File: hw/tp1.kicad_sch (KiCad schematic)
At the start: 27 parts

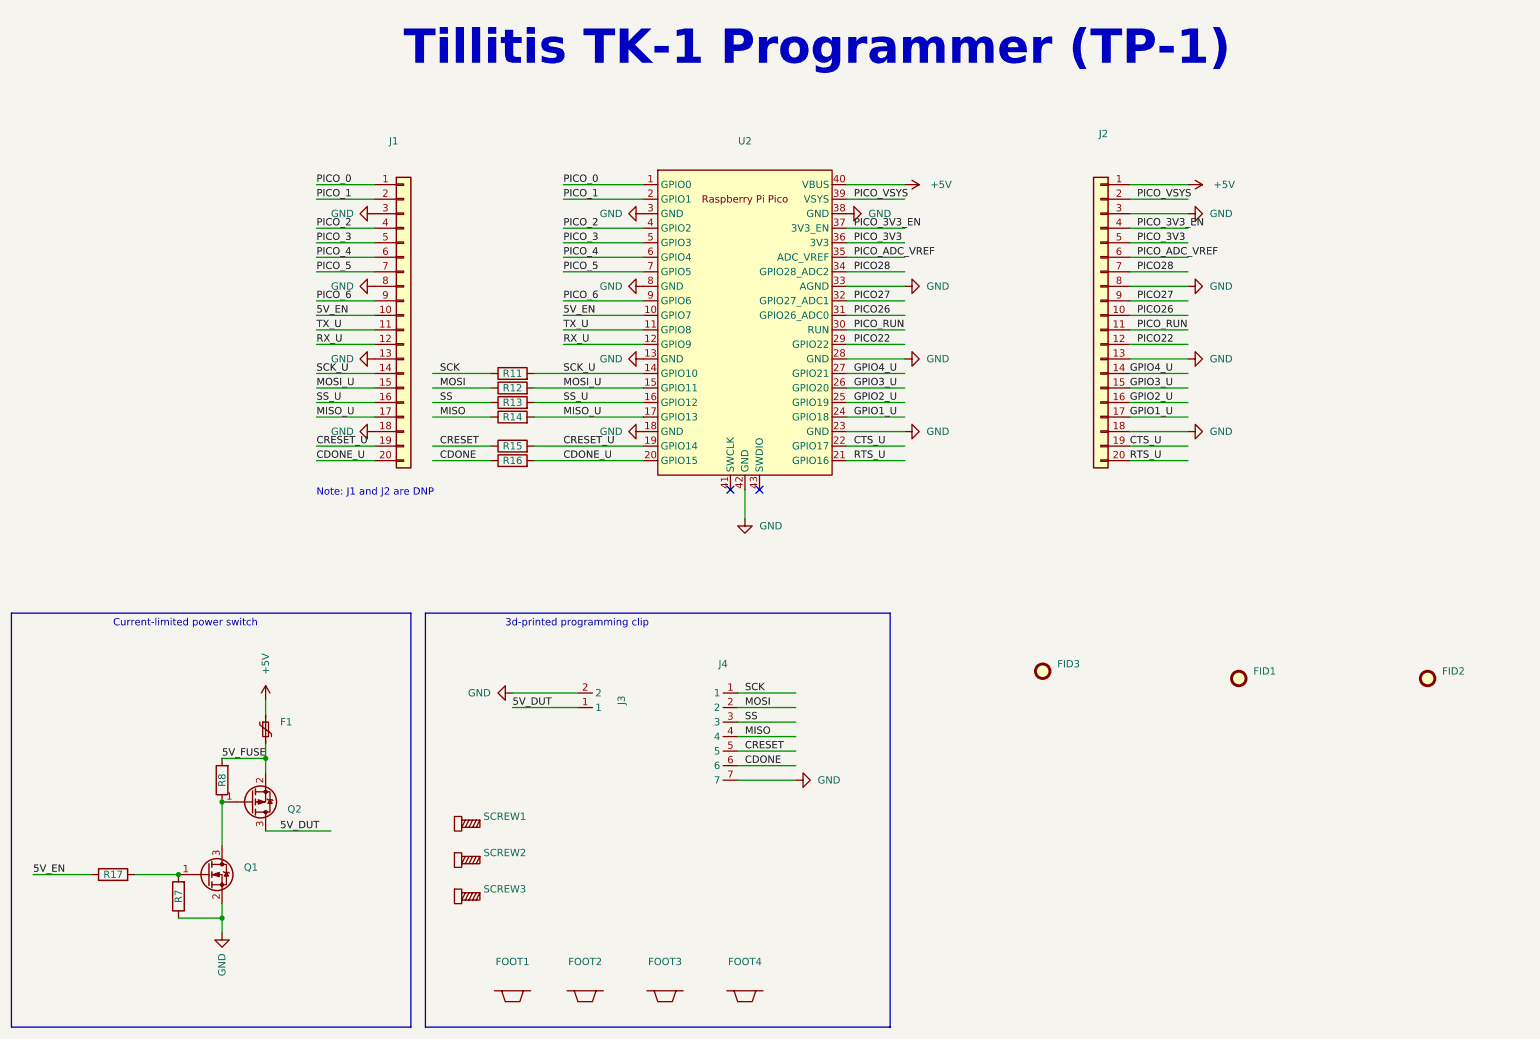
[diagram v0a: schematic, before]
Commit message: Added mta1-library and updated project links
- Updated links to symbols, footprints, drawsheet, 3D models
- Made the links use project defines instead of being absolute
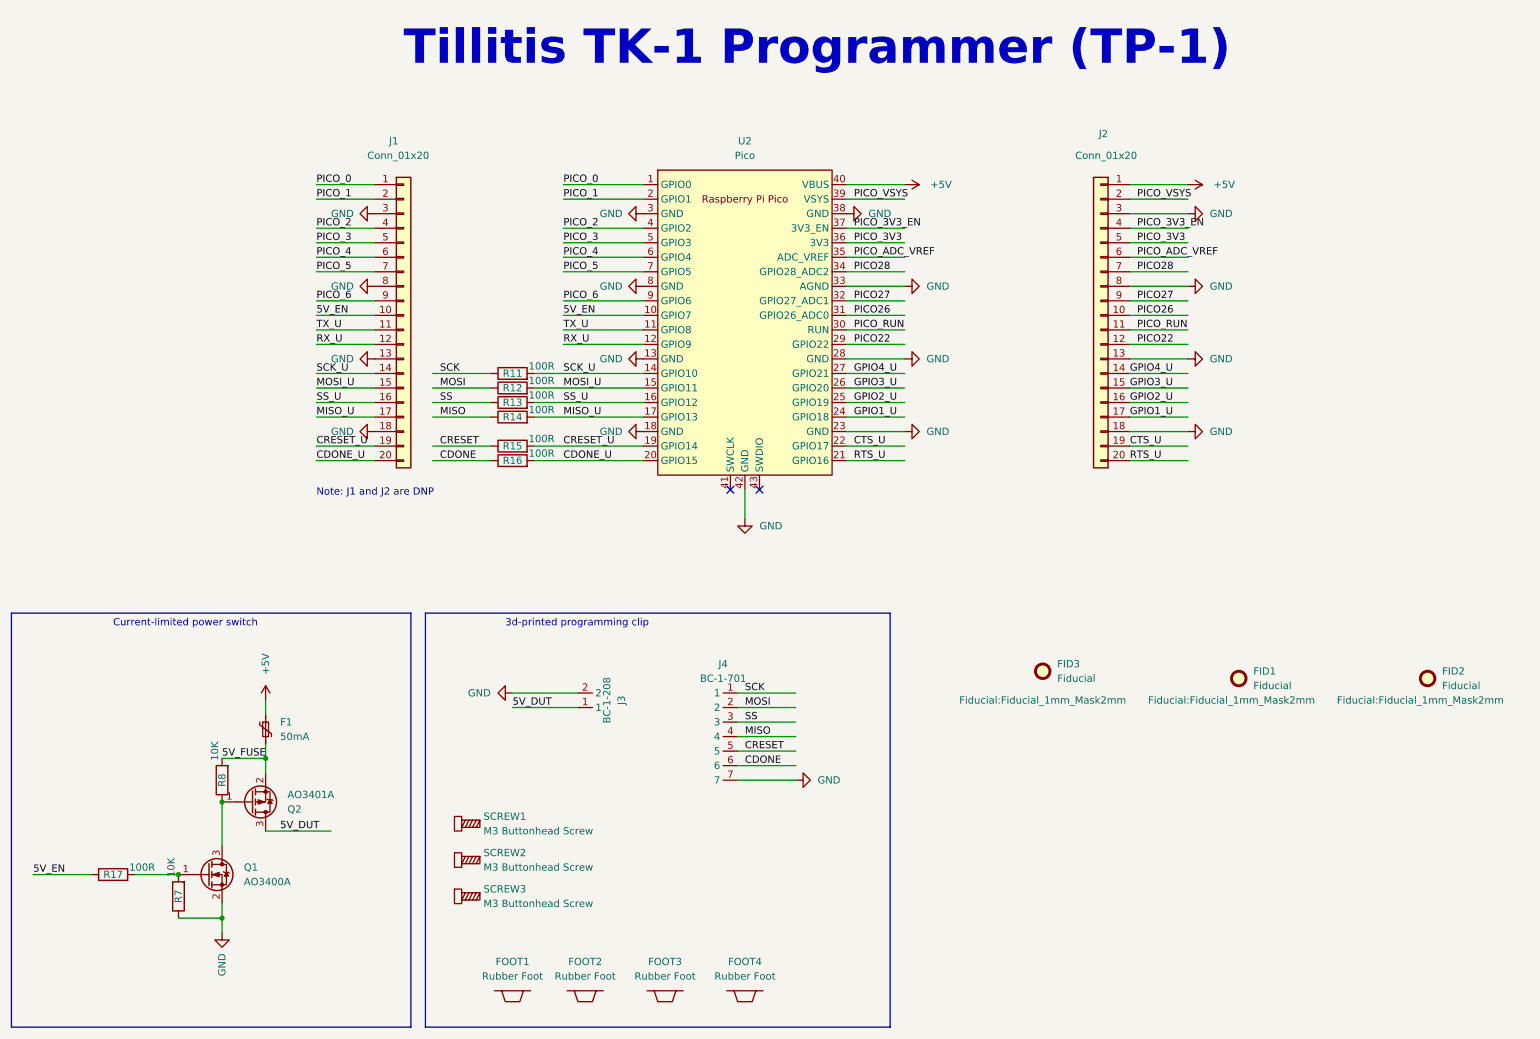
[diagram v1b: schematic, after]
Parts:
- F1: value (none) -> 50mA; footprint (none) -> Fuse:Fuse_1206_3216Metric
- FID1, FID2, FID3: value (none) -> Fiducial; footprint (none) -> Fiducial:Fiducial_1mm_Mask2mm
- FOOT1, FOOT2, FOOT3, FOOT4: value (none) -> Rubber Foot
- J1, J2: value (none) -> Conn_01x20; footprint (none) -> Connector_PinHeader_2.54mm:PinHeader_1x20_P2.54mm_Vertical
- J3: value (none) -> BC-1-208; footprint (none) -> mta1:BC-1-208
- J4: value (none) -> BC-1-701; footprint (none) -> mta1:BC-1-701
- Q1: value (none) -> AO3400A; footprint (none) -> Package_TO_SOT_SMD:SOT-23
- Q2: value (none) -> AO3401A; footprint (none) -> Package_TO_SOT_SMD:SOT-23
- R11, R12, R13, R14, R15, R16, R17: value (none) -> 100R; footprint (none) -> mta1:ERJ2G(0402)_L
- R7, R8: value (none) -> 10K; footprint (none) -> mta1:ERJ2G(0402)_L
- SCREW1, SCREW2, SCREW3: value (none) -> M3 Buttonhead Screw
- U2: value (none) -> Pico; footprint (none) -> MCU_RaspberryPi_and_Boards:RPi_Pico_SMD_reflow

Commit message: Fix all ERC errors.
- Update symbols
- Add PWR_FLAG
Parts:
- U2: footprint MCU_RaspberryPi_and_Boards:RPi_Pico_SMD_reflow -> RPi_Pico:RPi_Pico_SMD_TH
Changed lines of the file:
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@@
     (comment 2 "https://github.com/tillitis/tp1")
   )
+  (junction (at 143.51 104.14) (diameter 0) (color 0 0 0 0)
+  )
   (junction (at 52.07 173.99) (diameter 0) (color 0 0 0 0)
   )
   (junction (at 44.45 166.37) (diameter 0) (color 0 0 0 0)
+  )
+  (junction (at 165.1 45.72) (diameter 0) (color 0 0 0 0)
   )
   (junction (at 52.07 153.67) (diameter 0) (color 0 0 0 0)
@@
     (stroke (width 0) (type default))
   )
-  (wire (pts (xy 161.29 58.42) (xy 171.45 58.42))
+  (wire (pts (xy 161.29 58.42) (xy 176.53 58.42))
     (stroke (width 0) (type default))
   )
@@
     (stroke (width 0) (type default))
   )
+  (wire (pts (xy 161.29 55.88) (xy 176.53 55.88))
+    (stroke (width 0) (type default))
+  )
   (wire (pts (xy 88.9 81.28) (xy 99.06 81.28))
     (stroke (width 0) (type default))
@@
     (stroke (width 0) (type default))
   )
-  (wire (pts (xy 161.29 48.26) (xy 171.45 48.26))
+  (wire (pts (xy 161.29 48.26) (xy 176.53 48.26))
     (stroke (width 0) (type default))
   )
@@
     (stroke (width 0) (type default))
   )
-  (wire (pts (xy 161.29 55.88) (xy 171.45 55.88))
-    (stroke (width 0) (type default))
-  )
   (wire (pts (xy 161.29 83.82) (xy 171.45 83.82))
     (stroke (width 0) (type default))
@@
     (stroke (width 0) (type default))
   )
-  (wire (pts (xy 161.29 45.72) (xy 171.45 45.72))
+  (wire (pts (xy 161.29 45.72) (xy 165.1 45.72))
     (stroke (width 0) (type default))
   )
@@
   )
   (wire (pts (xy 142.24 147.32) (xy 152.4 147.32))
+    (stroke (width 0) (type default))
+  )
+  (wire (pts (xy 165.1 45.72) (xy 167.64 45.72))
     (stroke (width 0) (type default))
   )
@@
       (effects (font (size 1.27 1.27)))
     )
-    (property "Footprint" "MCU_RaspberryPi_and_Boards:RPi_Pico_SMD_reflow" (at 143.51 69.85 90)
+    (property "Footprint" "RPi_Pico:RPi_Pico_SMD_TH" (at 143.51 69.85 90)
       (effects (font (size 1.27 1.27)) hide)
     )
@@
     )
     (property "Supplier Part Number" "2648-SC0915TR-ND" (at 143.51 69.85 0)
+      (effects (font (size 1.27 1.27)) hide)
+    )
+    (property "Component" "" (at 143.51 69.85 0)
+      (effects (font (size 1.27 1.27)) hide)
+    )
+    (property "Rating" "" (at 143.51 69.85 0)
+      (effects (font (size 1.27 1.27)) hide)
+    )
+    (property "Package" "" (at 143.51 69.85 0)
+      (effects (font (size 1.27 1.27)) hide)
+    )
+    (property "Or equivalent" "" (at 143.51 69.85 0)
       (effects (font (size 1.27 1.27)) hide)
     )
@@
     )
   )
+  (symbol (lib_id "power:PWR_FLAG") (at 176.53 55.88 0) (unit 1)
+    (in_bom yes) (on_board yes) (dnp no)
+    (property "Reference" "#FLG04" (at 176.53 53.975 0)
+      (effects (font (size 1.27 1.27)) hide)
+    )
+    (property "Value" "PWR_FLAG" (at 181.61 52.07 0)
+      (effects (font (size 1.27 1.27)) hide)
+    )
+    (property "Footprint" "" (at 176.53 55.88 0)
+      (effects (font (size 1.27 1.27)) hide)
+    )
+    (property "Datasheet" "~" (at 176.53 55.88 0)
+      (effects (font (size 1.27 1.27)) hide)
+    )
+    (pin "1")
+    (instances
+      (project "tp1"
+        (path "/b5fbde6a-5a24-47bc-a5df-ebb462e219ef"
+          (reference "#FLG04") (unit 1)
+        )
+      )
+    )
+  )
+  (symbol (lib_id "power:PWR_FLAG") (at 176.53 58.42 180) (unit 1)
+    (in_bom yes) (on_board yes) (dnp no)
+    (property "Reference" "#FLG05" (at 176.53 60.325 0)
+      (effects (font (size 1.27 1.27)) hide)
+    )
+    (property "Value" "PWR_FLAG" (at 170.18 60.96 0)
+      (effects (font (size 1.27 1.27)) hide)
+    )
+    (property "Footprint" "" (at 176.53 58.42 0)
+      (effects (font (size 1.27 1.27)) hide)
+    )
+    (property "Datasheet" "~" (at 176.53 58.42 0)
+      (effects (font (size 1.27 1.27)) hide)
+    )
+    (pin "1")
+    (instances
+      (project "tp1"
+        (path "/b5fbde6a-5a24-47bc-a5df-ebb462e219ef"
+          (reference "#FLG05") (unit 1)
+        )
+      )
+    )
+  )
   (symbol (lib_id "power:GND") (at 78.74 63.5 270) (unit 1)
     (in_bom yes) (on_board yes) (dnp no)
@@
     )
   )
+  (symbol (lib_id "power:PWR_FLAG") (at 176.53 48.26 0) (unit 1)
+    (in_bom yes) (on_board yes) (dnp no)
+    (property "Reference" "#FLG03" (at 176.53 46.355 0)
+      (effects (font (size 1.27 1.27)) hide)
+    )
+    (property "Value" "PWR_FLAG" (at 180.34 44.45 0)
+      (effects (font (size 1.27 1.27)) hide)
+    )
+    (property "Footprint" "" (at 176.53 48.26 0)
+      (effects (font (size 1.27 1.27)) hide)
+    )
+    (property "Datasheet" "~" (at 176.53 48.26 0)
+      (effects (font (size 1.27 1.27)) hide)
+    )
+    (pin "1")
+    (instances
+      (project "tp1"
+        (path "/b5fbde6a-5a24-47bc-a5df-ebb462e219ef"
+          (reference "#FLG03") (unit 1)
+        )
+      )
+    )
+  )
   (symbol (lib_id "Transistor_FET:AO3400A") (at 49.53 166.37 0) (unit 1)
     (in_bom yes) (on_board yes) (dnp no) (fields_autoplaced)
@@
     )
   )
+  (symbol (lib_id "power:PWR_FLAG") (at 165.1 45.72 0) (unit 1)
+    (in_bom yes) (on_board yes) (dnp no) (fields_autoplaced)
+    (property "Reference" "#FLG01" (at 165.1 43.815 0)
+      (effects (font (size 1.27 1.27)) hide)
+    )
+    (property "Value" "PWR_FLAG" (at 165.1 40.64 0)
+      (effects (font (size 1.27 1.27)) hide)
+    )
+    (property "Footprint" "" (at 165.1 45.72 0)
+      (effects (font (size 1.27 1.27)) hide)
+    )
+    (property "Datasheet" "~" (at 165.1 45.72 0)
+      (effects (font (size 1.27 1.27)) hide)
+    )
+    (pin "1")
+    (instances
+      (project "tp1"
+        (path "/b5fbde6a-5a24-47bc-a5df-ebb462e219ef"
+          (reference "#FLG01") (unit 1)
+        )
+      )
+    )
+  )
   (symbol (lib_id "Device:R") (at 33.02 166.37 90) (unit 1)
     (in_bom yes) (on_board yes) (dnp no)
@@
     )
     (property "Datasheet" "" (at 143.51 104.14 0)
+      (effects (font (size 1.27 1.27)) hide)
+    )
+    (property "Component" "" (at 143.51 104.14 0)
+      (effects (font (size 1.27 1.27)) hide)
+    )
+    (property "Rating" "" (at 143.51 104.14 0)
+      (effects (font (size 1.27 1.27)) hide)
+    )
+    (property "Package" "" (at 143.51 104.14 0)
+      (effects (font (size 1.27 1.27)) hide)
+    )
+    (property "Manufacturer" "" (at 143.51 104.14 0)
+      (effects (font (size 1.27 1.27)) hide)
+    )
+    (property "Manufacturer Part Number" "" (at 143.51 104.14 0)
+      (effects (font (size 1.27 1.27)) hide)
+    )
+    (property "Supplier" "" (at 143.51 104.14 0)
+      (effects (font (size 1.27 1.27)) hide)
+    )
+    (property "Supplier Part Number" "" (at 143.51 104.14 0)
+      (effects (font (size 1.27 1.27)) hide)
+    )
+    (property "Or equivalent" "" (at 143.51 104.14 0)
       (effects (font (size 1.27 1.27)) hide)
     )
@@
     )
   )
-  (symbol (lib_id "power:+5V") (at 171.45 45.72 270) (unit 1)
-    (in_bom yes) (on_board yes) (dnp no)
-    (property "Reference" "#PWR07" (at 167.64 45.72 0)
-      (effects (font (size 1.27 1.27)) hide)
-    )
-    (property "Value" "+5V" (at 177.8 45.72 90)
-      (effects (font (size 1.27 1.27)))
-    )
-    (property "Footprint" "" (at 171.45 45.72 0)
-      (effects (font (size 1.27 1.27)) hide)
-    )
-    (property "Datasheet" "" (at 171.45 45.72 0)
+  (symbol (lib_id "power:+5V") (at 167.64 45.72 0) (unit 1)
+    (in_bom yes) (on_board yes) (dnp no)
+    (property "Reference" "#PWR07" (at 167.64 49.53 0)
+      (effects (font (size 1.27 1.27)) hide)
+    )
+    (property "Value" "+5V" (at 167.64 41.91 0)
+      (effects (font (size 1.27 1.27)))
+    )
+    (property "Footprint" "" (at 167.64 45.72 0)
+      (effects (font (size 1.27 1.27)) hide)
+    )
+    (property "Datasheet" "" (at 167.64 45.72 0)
       (effects (font (size 1.27 1.27)) hide)
     )
@@
         )
       )
+    )
+  )
+  (symbol (lib_id "power:PWR_FLAG") (at 143.51 104.14 90) (unit 1)
+    (in_bom yes) (on_board yes) (dnp no) (fields_autoplaced)
+    (property "Reference" "#FLG02" (at 141.605 104.14 0)
+      (effects (font (size 1.27 1.27)) hide)
+    )
+    (property "Value" "PWR_FLAG" (at 139.7 104.14 90)
+      (effects (font (size 1.27 1.27)) (justify left) hide)
+    )
+    (property "Footprint" "" (at 143.51 104.14 0)
+      (effects (font (size 1.27 1.27)) hide)
+    )
+    (property "Datasheet" "~" (at 143.51 104.14 0)
+      (effects (font (size 1.27 1.27)) hide)
+    )
+    (pin "1")
+    (instances
+      (project "tp1"
+        (path "/b5fbde6a-5a24-47bc-a5df-ebb462e219ef"
+          (reference "#FLG02") (unit 1)
+        )
+      )
